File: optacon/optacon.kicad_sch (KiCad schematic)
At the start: 17 parts, among them J1 Conn_01x12

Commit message: pcb + stencils ordered from pcbgogo
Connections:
- net REG: no longer TP11.1
- new net EN: TP11.1
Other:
- sheet hv_driver ports: added EN; removed none
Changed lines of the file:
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@@
+    (stroke (width 0) (type default) (color 0 0 0 0))
+  )
+  (wire (pts (xy 99.06 109.22) (xy 104.14 109.22))
     (stroke (width 0) (type default) (color 0 0 0 0))
   )
@@
     (effects (font (size 1.27 1.27)) (justify left bottom))
   )
-  (label "REG" (at 88.9 175.26 0)
+  (label "EN" (at 88.9 175.26 0)
     (effects (font (size 1.27 1.27)) (justify left bottom))
   )
   (label "VBST" (at 88.9 148.59 0)
     (effects (font (size 1.27 1.27)) (justify left bottom))
+  )
+  (label "EN" (at 99.06 109.22 180)
+    (effects (font (size 1.27 1.27)) (justify right bottom))
   )
   (label "VBIAS" (at 175.26 41.91 180)
@@
       (effects (font (size 1.27 1.27)) (justify right))
     )
-  )
+    (pin "EN" input (at 104.14 109.22 180)
+      (effects (font (size 1.27 1.27)) (justify left))
+    )
+  )

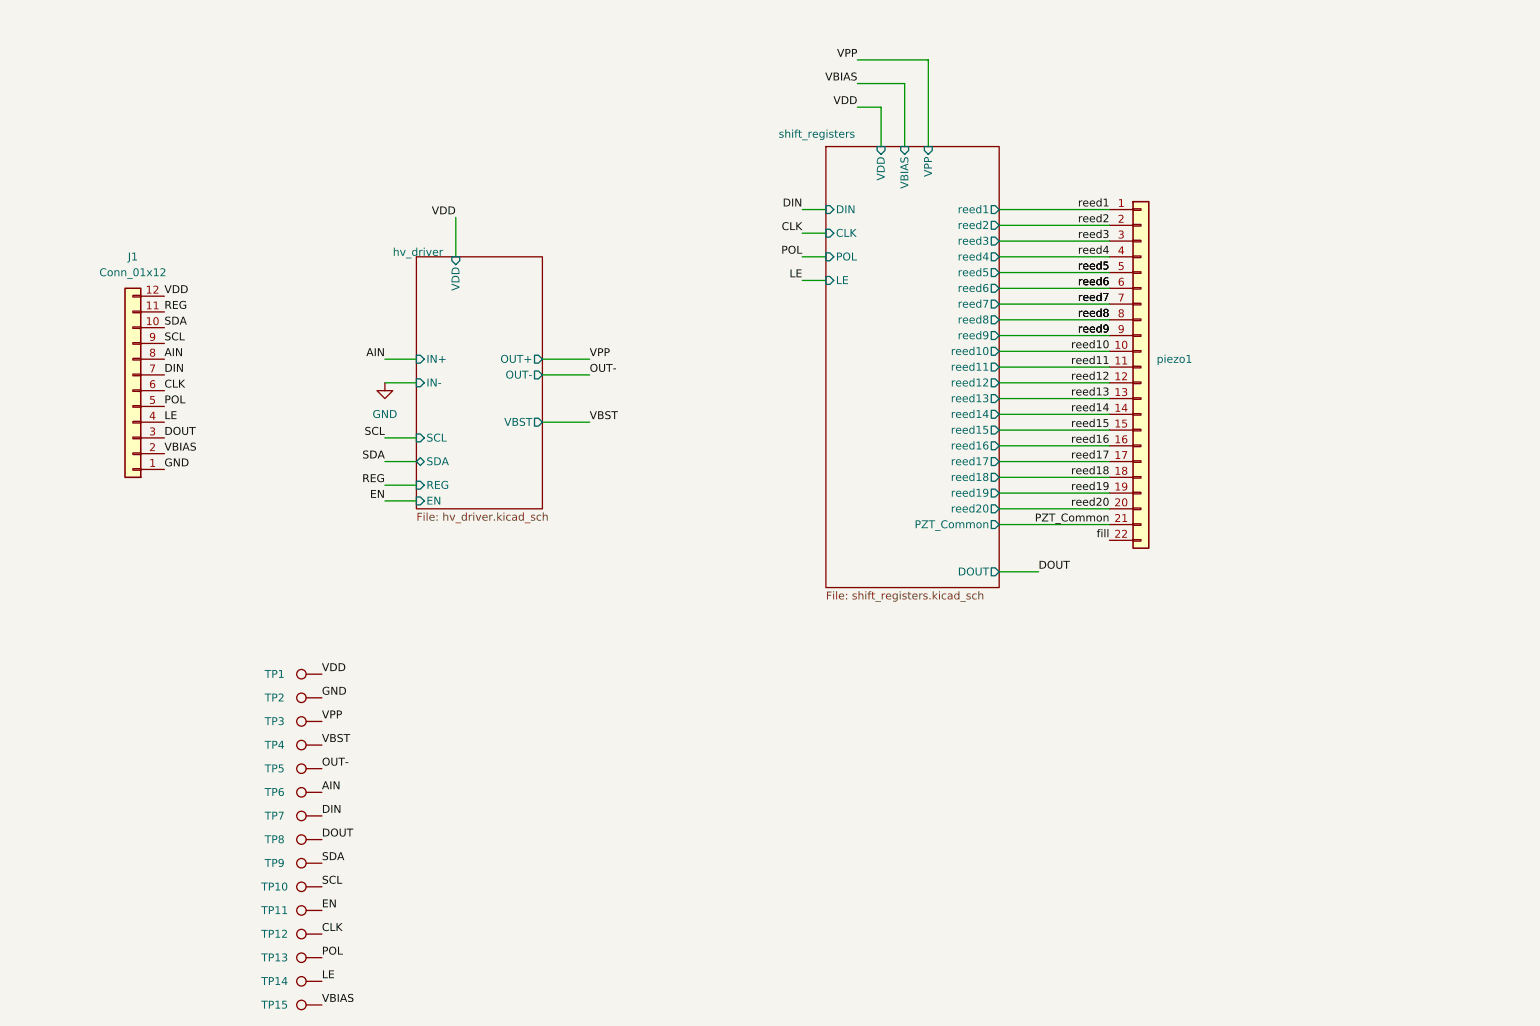
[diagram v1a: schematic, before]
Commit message: remove VBIAS, EN, REG rename & reorder nets for i2c, spi add IN- next to IN+ (AIN) add SMD FPC connector for piezo use BP instead of HVOUTs for piezo_common
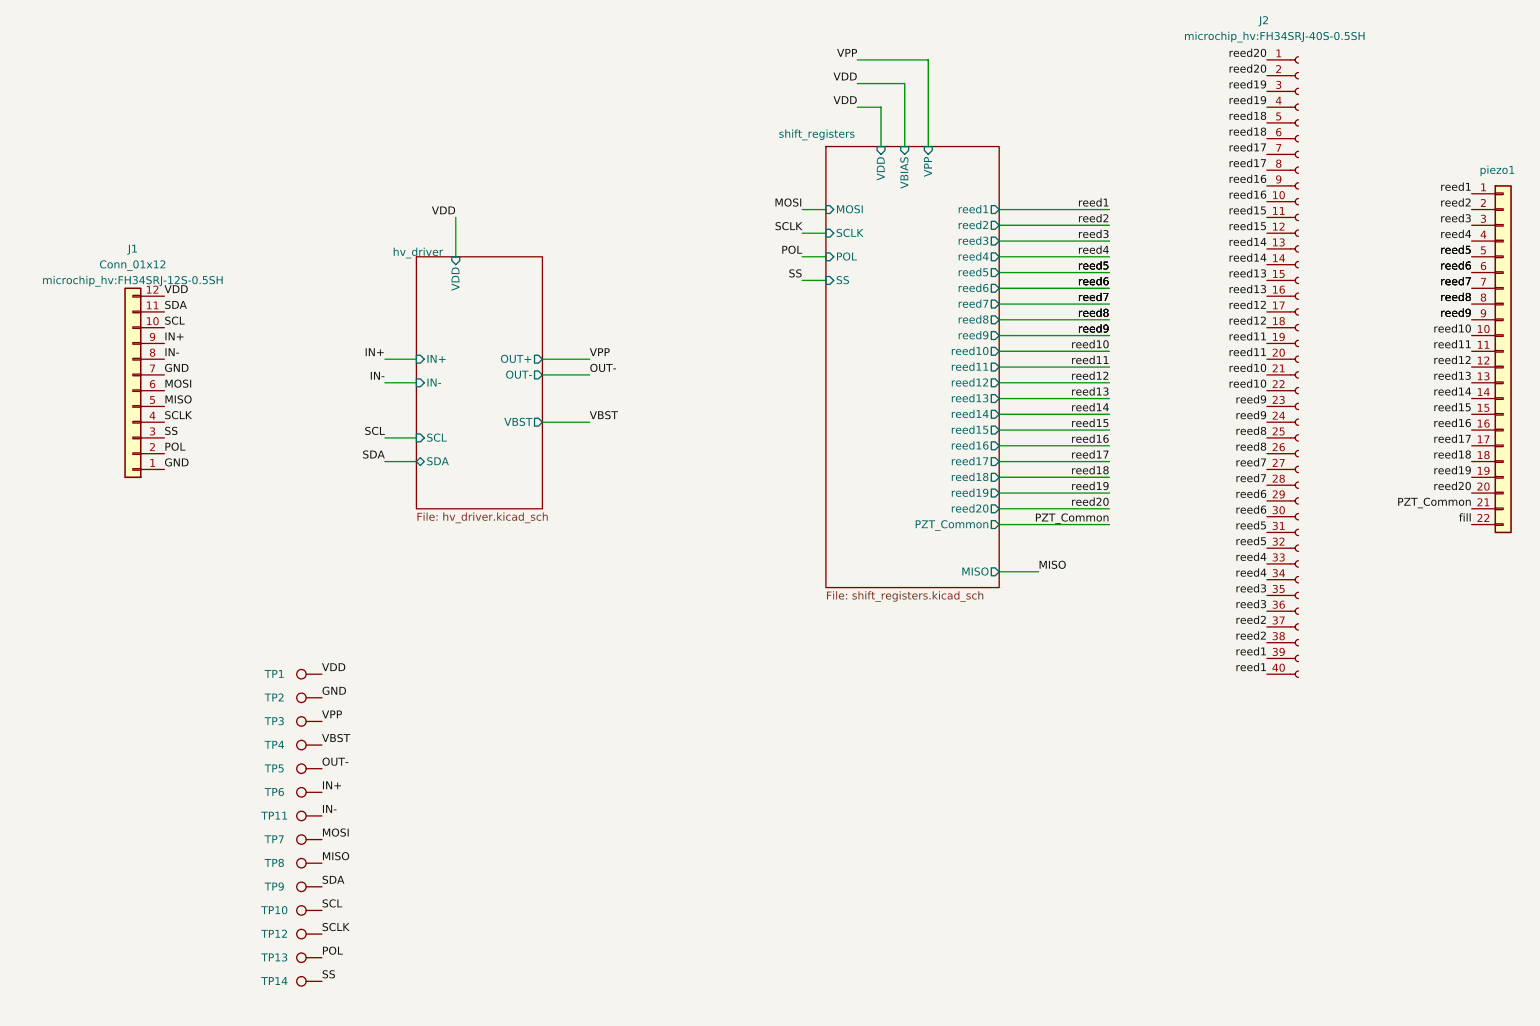
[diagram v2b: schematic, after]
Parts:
- removed TP15: TestPoint, TestPoint:TestPoint_Pad_D1.0mm, symbol Connector:TestPoint
- added J2: Conn_01x40_Socket, microchip_hv:FH34SRJ-40S-0.5SH, symbol Connector:Conn_01x40_Socket
- TP1, TP10, TP11, TP12, TP13, TP14, TP3, TP4, TP5, TP6, TP7, TP8, TP9: footprint TestPoint:TestPoint_Pad_D1.0mm -> TestPoint:TestPoint_THTPad_D1.0mm_Drill0.5mm
- TP2: footprint TestPoint:TestPoint_Pad_D1.0mm -> TestPoint:TestPoint_THTPad_1.0x1.0mm_Drill0.5mm
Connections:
- net REG is gone; now on net SDA: J1.11 (Pin_11)
- net VBIAS is gone; now on net POL: J1.2 (Pin_2)
- net GND: now also J1.7 (Pin_7)
- net POL: no longer J1.5 (Pin_5)
- net SCL: now also J1.10 (Pin_10); no longer J1.9 (Pin_9)
- net SDA: no longer J1.10 (Pin_10)
- net reed1: now also J2.39 (Pin_39), J2.40 (Pin_40)
- net reed10: now also J2.21 (Pin_21), J2.22 (Pin_22)
- net reed11: now also J2.19 (Pin_19), J2.20 (Pin_20)
- net reed12: now also J2.17 (Pin_17), J2.18 (Pin_18)
- net reed13: now also J2.15 (Pin_15), J2.16 (Pin_16)
- net reed14: now also J2.13 (Pin_13), J2.14 (Pin_14)
- net reed15: now also J2.11 (Pin_11), J2.12 (Pin_12)
- net reed16: now also J2.10 (Pin_10), J2.9 (Pin_9)
- net reed17: now also J2.7 (Pin_7), J2.8 (Pin_8)
- net reed18: now also J2.5 (Pin_5), J2.6 (Pin_6)
- net reed19: now also J2.3 (Pin_3), J2.4 (Pin_4)
- net reed2: now also J2.37 (Pin_37), J2.38 (Pin_38)
- net reed20: now also J2.1 (Pin_1), J2.2 (Pin_2)
- net reed3: now also J2.35 (Pin_35), J2.36 (Pin_36)
- net reed4: now also J2.33 (Pin_33), J2.34 (Pin_34)
- net reed5: now also J2.31 (Pin_31), J2.32 (Pin_32)
- net reed6: now also J2.29 (Pin_29), J2.30 (Pin_30)
- net reed7: now also J2.27 (Pin_27), J2.28 (Pin_28)
- net reed8: now also J2.25 (Pin_25), J2.26 (Pin_26)
- net reed9: now also J2.23 (Pin_23), J2.24 (Pin_24)
- net AIN renamed IN+
- net IN+: now also J1.9 (Pin_9); no longer J1.8 (Pin_8)
- net CLK renamed MOSI
- net MOSI: now also TP7.1; no longer TP12.1
- removed net DIN: J1.7 (Pin_7), TP7.1
- net DOUT renamed MISO
- net MISO: now also J1.5 (Pin_5); no longer J1.3 (Pin_3)
- net EN renamed IN-
- net IN-: now also J1.8 (Pin_8)
- net LE renamed SCLK
- net SCLK: now also TP12.1; no longer TP14.1
- new net SS: J1.3 (Pin_3), TP14.1
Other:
- sheet hv_driver ports: added none; removed EN, REG
- sheet shift_registers ports: added MISO, MOSI, SCLK, SS; removed CLK, DIN, DOUT, LE
- moved on the sheet: TP10, TP7, TP8, TP9, piezo1

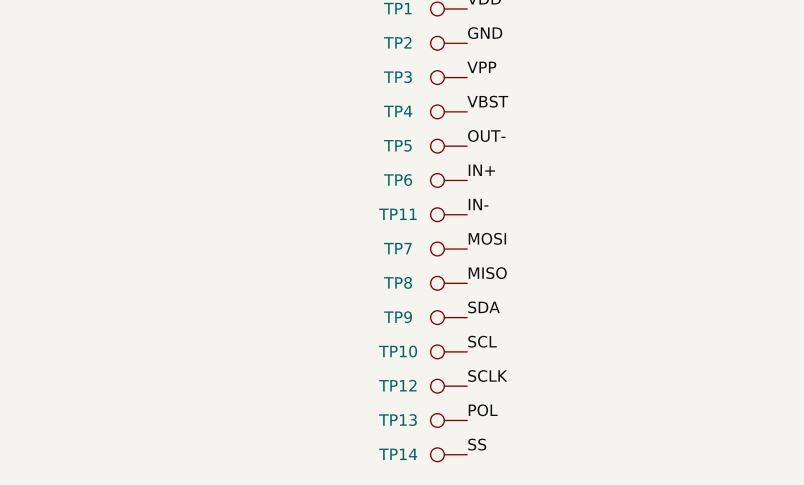
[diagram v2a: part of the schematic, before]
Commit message: J2 (mounting) pads no paste
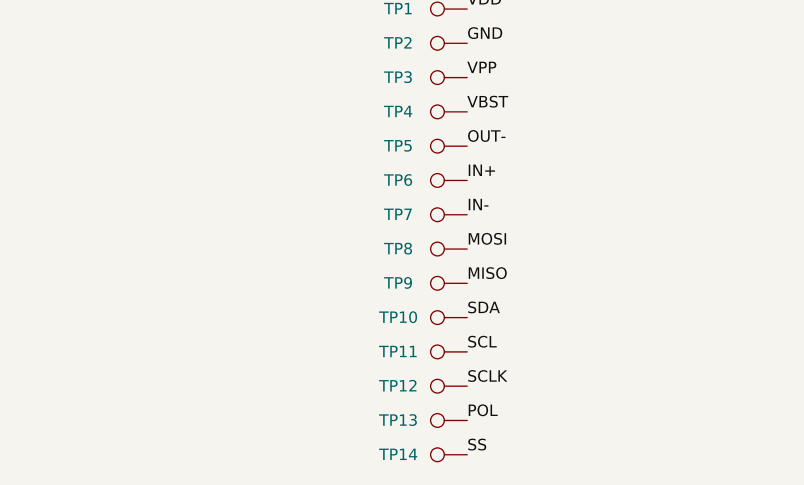
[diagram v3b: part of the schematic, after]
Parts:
- renumbered TP9 to TP10, TP10 to TP11, TP11 to TP7, TP7 to TP8, TP8 to TP9
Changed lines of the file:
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@@
   (symbol (lib_id "Connector:TestPoint") (at 88.9 175.26 90) (unit 1)
     (in_bom yes) (on_board yes) (dnp no)
-    (property "Reference" "TP10" (at 81.28 175.26 90)
+    (property "Reference" "TP11" (at 81.28 175.26 90)
       (effects (font (size 1.27 1.27)))
     )
@@
       (project "optacon"
         (path "/e63e39d7-6ac0-4ffd-8aa3-1841a4541b55"
-          (reference "TP10") (unit 1)
+          (reference "TP11") (unit 1)
         )
       )
@@
   (symbol (lib_id "Connector:TestPoint") (at 88.9 171.45 90) (unit 1)
     (in_bom yes) (on_board yes) (dnp no)
-    (property "Reference" "TP9" (at 81.28 171.45 90)
+    (property "Reference" "TP10" (at 81.28 171.45 90)
       (effects (font (size 1.27 1.27)))
     )
@@
       (project "optacon"
         (path "/e63e39d7-6ac0-4ffd-8aa3-1841a4541b55"
+          (reference "TP10") (unit 1)
+        )
+      )
+    )
+  )
+  (symbol (lib_id "Connector:TestPoint") (at 88.9 152.4 90) (unit 1)
+    (in_bom yes) (on_board yes) (dnp no)
+    (property "Reference" "TP5" (at 81.28 152.4 90)
+      (effects (font (size 1.27 1.27)))
+    )
+    (property "Value" "TestPoint" (at 95.25 152.4 90)
+      (effects (font (size 1.27 1.27)) hide)
+    )
+    (property "Footprint" "TestPoint:TestPoint_THTPad_D1.0mm_Drill0.5mm" (at 88.9 147.32 0)
+      (effects (font (size 1.27 1.27)) hide)
+    )
+    (property "Datasheet" "~" (at 88.9 147.32 0)
+      (effects (font (size 1.27 1.27)) hide)
+    )
+    (pin "1")
+    (instances
+      (project "optacon"
+        (path "/e63e39d7-6ac0-4ffd-8aa3-1841a4541b55"
+          (reference "TP5") (unit 1)
+        )
+      )
+    )
+  )
+  (symbol (lib_id "Connector:TestPoint") (at 88.9 167.64 90) (unit 1)
+    (in_bom yes) (on_board yes) (dnp no)
+    (property "Reference" "TP9" (at 81.28 167.64 90)
+      (effects (font (size 1.27 1.27)))
+    )
+    (property "Value" "TestPoint" (at 95.25 167.64 90)
+      (effects (font (size 1.27 1.27)) hide)
+    )
+    (property "Footprint" "TestPoint:TestPoint_THTPad_D1.0mm_Drill0.5mm" (at 88.9 162.56 0)
+      (effects (font (size 1.27 1.27)) hide)
+    )
+    (property "Datasheet" "~" (at 88.9 162.56 0)
+      (effects (font (size 1.27 1.27)) hide)
+    )
+    (pin "1")
+    (instances
+      (project "optacon"
+        (path "/e63e39d7-6ac0-4ffd-8aa3-1841a4541b55"
           (reference "TP9") (unit 1)
-        )
-      )
-    )
-  )
-  (symbol (lib_id "Connector:TestPoint") (at 88.9 152.4 90) (unit 1)
-    (in_bom yes) (on_board yes) (dnp no)
-    (property "Reference" "TP5" (at 81.28 152.4 90)
-      (effects (font (size 1.27 1.27)))
-    )
-    (property "Value" "TestPoint" (at 95.25 152.4 90)
-      (effects (font (size 1.27 1.27)) hide)
-    )
-    (property "Footprint" "TestPoint:TestPoint_THTPad_D1.0mm_Drill0.5mm" (at 88.9 147.32 0)
-      (effects (font (size 1.27 1.27)) hide)
-    )
-    (property "Datasheet" "~" (at 88.9 147.32 0)
-      (effects (font (size 1.27 1.27)) hide)
-    )
-    (pin "1")
-    (instances
-      (project "optacon"
-        (path "/e63e39d7-6ac0-4ffd-8aa3-1841a4541b55"
-          (reference "TP5") (unit 1)
-        )
-      )
-    )
-  )
-  (symbol (lib_id "Connector:TestPoint") (at 88.9 167.64 90) (unit 1)
-    (in_bom yes) (on_board yes) (dnp no)
-    (property "Reference" "TP8" (at 81.28 167.64 90)
-      (effects (font (size 1.27 1.27)))
-    )
-    (property "Value" "TestPoint" (at 95.25 167.64 90)
-      (effects (font (size 1.27 1.27)) hide)
-    )
-    (property "Footprint" "TestPoint:TestPoint_THTPad_D1.0mm_Drill0.5mm" (at 88.9 162.56 0)
-      (effects (font (size 1.27 1.27)) hide)
-    )
-    (property "Datasheet" "~" (at 88.9 162.56 0)
-      (effects (font (size 1.27 1.27)) hide)
-    )
-    (pin "1")
-    (instances
-      (project "optacon"
-        (path "/e63e39d7-6ac0-4ffd-8aa3-1841a4541b55"
-          (reference "TP8") (unit 1)
         )
       )
@@
   (symbol (lib_id "Connector:TestPoint") (at 88.9 163.83 90) (unit 1)
     (in_bom yes) (on_board yes) (dnp no)
-    (property "Reference" "TP7" (at 81.28 163.83 90)
+    (property "Reference" "TP8" (at 81.28 163.83 90)
       (effects (font (size 1.27 1.27)))
     )
@@
       (project "optacon"
         (path "/e63e39d7-6ac0-4ffd-8aa3-1841a4541b55"
+          (reference "TP8") (unit 1)
+        )
+      )
+    )
+  )
+  (symbol (lib_id "Connector:TestPoint") (at 88.9 140.97 90) (unit 1)
+    (in_bom yes) (on_board yes) (dnp no)
+    (property "Reference" "TP2" (at 81.28 140.97 90)
+      (effects (font (size 1.27 1.27)))
+    )
+    (property "Value" "TestPoint" (at 95.25 140.97 90)
+      (effects (font (size 1.27 1.27)) hide)
+    )
+    (property "Footprint" "TestPoint:TestPoint_THTPad_1.0x1.0mm_Drill0.5mm" (at 88.9 135.89 0)
+      (effects (font (size 1.27 1.27)) hide)
+    )
+    (property "Datasheet" "~" (at 88.9 135.89 0)
+      (effects (font (size 1.27 1.27)) hide)
+    )
+    (pin "1")
+    (instances
+      (project "optacon"
+        (path "/e63e39d7-6ac0-4ffd-8aa3-1841a4541b55"
+          (reference "TP2") (unit 1)
+        )
+      )
+    )
+  )
+  (symbol (lib_id "Connector:TestPoint") (at 88.9 144.78 90) (unit 1)
+    (in_bom yes) (on_board yes) (dnp no)
+    (property "Reference" "TP3" (at 81.28 144.78 90)
+      (effects (font (size 1.27 1.27)))
+    )
+    (property "Value" "TestPoint" (at 95.25 144.78 90)
+      (effects (font (size 1.27 1.27)) hide)
+    )
+    (property "Footprint" "TestPoint:TestPoint_THTPad_D1.0mm_Drill0.5mm" (at 88.9 139.7 0)
+      (effects (font (size 1.27 1.27)) hide)
+    )
+    (property "Datasheet" "~" (at 88.9 139.7 0)
+      (effects (font (size 1.27 1.27)) hide)
+    )
+    (pin "1")
+    (instances
+      (project "optacon"
+        (path "/e63e39d7-6ac0-4ffd-8aa3-1841a4541b55"
+          (reference "TP3") (unit 1)
+        )
+      )
+    )
+  )
+  (symbol (lib_id "Connector:TestPoint") (at 88.9 160.02 90) (unit 1)
+    (in_bom yes) (on_board yes) (dnp no)
+    (property "Reference" "TP7" (at 81.28 160.02 90)
+      (effects (font (size 1.27 1.27)))
+    )
+    (property "Value" "TestPoint" (at 95.25 160.02 90)
+      (effects (font (size 1.27 1.27)) hide)
+    )
+    (property "Footprint" "TestPoint:TestPoint_THTPad_D1.0mm_Drill0.5mm" (at 88.9 154.94 0)
+      (effects (font (size 1.27 1.27)) hide)
+    )
+    (property "Datasheet" "~" (at 88.9 154.94 0)
+      (effects (font (size 1.27 1.27)) hide)
+    )
+    (pin "1")
+    (instances
+      (project "optacon"
+        (path "/e63e39d7-6ac0-4ffd-8aa3-1841a4541b55"
           (reference "TP7") (unit 1)
         )
       )
-    )
-  )
-  (symbol (lib_id "Connector:TestPoint") (at 88.9 140.97 90) (unit 1)
-    (in_bom yes) (on_board yes) (dnp no)
-    (property "Reference" "TP2" (at 81.28 140.97 90)
-      (effects (font (size 1.27 1.27)))
-    )
-    (property "Value" "TestPoint" (at 95.25 140.97 90)
-      (effects (font (size 1.27 1.27)) hide)
-    )
-    (property "Footprint" "TestPoint:TestPoint_THTPad_1.0x1.0mm_Drill0.5mm" (at 88.9 135.89 0)
-      (effects (font (size 1.27 1.27)) hide)
-    )
-    (property "Datasheet" "~" (at 88.9 135.89 0)
-      (effects (font (size 1.27 1.27)) hide)
-    )
-    (pin "1")
-    (instances
-      (project "optacon"
-        (path "/e63e39d7-6ac0-4ffd-8aa3-1841a4541b55"
-          (reference "TP2") (unit 1)
-        )
-      )
-    )
-  )
-  (symbol (lib_id "Connector:TestPoint") (at 88.9 144.78 90) (unit 1)
-    (in_bom yes) (on_board yes) (dnp no)
-    (property "Reference" "TP3" (at 81.28 144.78 90)
-      (effects (font (size 1.27 1.27)))
-    )
-    (property "Value" "TestPoint" (at 95.25 144.78 90)
-      (effects (font (size 1.27 1.27)) hide)
-    )
-    (property "Footprint" "TestPoint:TestPoint_THTPad_D1.0mm_Drill0.5mm" (at 88.9 139.7 0)
-      (effects (font (size 1.27 1.27)) hide)
-    )
-    (property "Datasheet" "~" (at 88.9 139.7 0)
-      (effects (font (size 1.27 1.27)) hide)
-    )
-    (pin "1")
-    (instances
-      (project "optacon"
-        (path "/e63e39d7-6ac0-4ffd-8aa3-1841a4541b55"
-          (reference "TP3") (unit 1)
-        )
-      )
-    )
-  )
-  (symbol (lib_id "Connector:TestPoint") (at 88.9 160.02 90) (unit 1)
-    (in_bom yes) (on_board yes) (dnp no)
-    (property "Reference" "TP11" (at 81.28 160.02 90)
-      (effects (font (size 1.27 1.27)))
-    )
-    (property "Value" "TestPoint" (at 95.25 160.02 90)
-      (effects (font (size 1.27 1.27)) hide)
-    )
-    (property "Footprint" "TestPoint:TestPoint_THTPad_D1.0mm_Drill0.5mm" (at 88.9 154.94 0)
-      (effects (font (size 1.27 1.27)) hide)
-    )
-    (property "Datasheet" "~" (at 88.9 154.94 0)
-      (effects (font (size 1.27 1.27)) hide)
-    )
-    (pin "1")
-    (instances
-      (project "optacon"
-        (path "/e63e39d7-6ac0-4ffd-8aa3-1841a4541b55"
-          (reference "TP11") (unit 1)
-        )
-      )
